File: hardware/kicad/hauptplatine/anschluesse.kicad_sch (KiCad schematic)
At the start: 9 parts, among them J701 DS18B20 Nr. 1, J702 DS18B20 Nr. 2, J703 BME280, J704 Erweiterung

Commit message: update
Footprints BQ25185, Ra-01SH, DEGSON 15EDGRC-3.5 (2-6P) in Bienen.pretty; HW-02 Akkuhalter Keystone 1042 SMD; SCH26-13 Klemmen einreihig mit LCSC-Nummern. Tests: ERC 0, Pin/Footprint 0 Abweichungen, Netzprüfung 178/178, alle_tests_linux.sh rc=0
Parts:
- J701, J702: footprint Connector_Phoenix_MC:PhoenixContact_MC_1,5_3-G-3.5_1x03_P3.50mm_Horizontal -> Bienen:DEGSON_15EDGRC-3.5-03P; LCSC (none) -> C5160226
- J703: footprint Connector_Phoenix_MC:PhoenixContact_MC_1,5_6-G-3.5_1x06_P3.50mm_Horizontal -> Bienen:DEGSON_15EDGRC-3.5-06P; LCSC (none) -> C49352918
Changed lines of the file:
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@@
 			)
 		)
-		(property "Footprint" "Connector_Phoenix_MC:PhoenixContact_MC_1,5_3-G-3.5_1x03_P3.50mm_Horizontal"
+		(property "Footprint" "Bienen:DEGSON_15EDGRC-3.5-03P"
 			(at 40.64 91.44 0)
 			(hide yes)
@@
 			)
 		)
-		(property "Description" "= J6 (TempIn): 1 GND, 2 DQ, 3 3V3_SW; DEGSON 15EDGRHC-3.5 3-polig (Platzhalter-Footprint Phoenix MC) [P]"
+		(property "Description" "= J6 (TempIn): 1 GND, 2 DQ, 3 3V3_SW; DEGSON 15EDGRC-3.5-03P"
+			(at 40.64 91.44 0)
+			(hide yes)
+			(show_name no)
+			(do_not_autoplace no)
+			(effects
+				(font
+					(size 1.27 1.27)
+				)
+			)
+		)
+		(property "LCSC" "C5160226"
 			(at 40.64 91.44 0)
 			(hide yes)
@@
 			)
 		)
-		(property "Footprint" "Connector_Phoenix_MC:PhoenixContact_MC_1,5_6-G-3.5_1x06_P3.50mm_Horizontal"
+		(property "Footprint" "Bienen:DEGSON_15EDGRC-3.5-06P"
 			(at 40.64 165.1 0)
 			(hide yes)
@@
 			)
 		)
-		(property "Description" "= J8: 1 Schirm, 2 GND, 3 SDA, 4 SCL, 5 3V3_SW, 6 frei (Verwechslungsschutz gegen J4, 6-polig); DEGSON 15EDGRHC-3.5 6-polig (Platzhalter-Footprint Phoenix MC) [P]"
+		(property "Description" "= J8: 1 Schirm, 2 GND, 3 SDA, 4 SCL, 5 3V3_SW, 6 frei (Verwechslungsschutz gegen J4, 6-polig); DEGSON 15EDGRC-3.5-06P"
+			(at 40.64 165.1 0)
+			(hide yes)
+			(show_name no)
+			(do_not_autoplace no)
+			(effects
+				(font
+					(size 1.27 1.27)
+				)
+			)
+		)
+		(property "LCSC" "C49352918"
 			(at 40.64 165.1 0)
 			(hide yes)
@@
 			)
 		)
-		(property "Footprint" "Connector_Phoenix_MC:PhoenixContact_MC_1,5_3-G-3.5_1x03_P3.50mm_Horizontal"
+		(property "Footprint" "Bienen:DEGSON_15EDGRC-3.5-03P"
 			(at 40.64 116.84 0)
 			(hide yes)
@@
 			)
 		)
-		(property "Description" "= J7 (TempIn2), selber Bus; DEGSON 15EDGRHC-3.5 3-polig (Platzhalter-Footprint Phoenix MC) [P]"
+		(property "Description" "= J7 (TempIn2), selber Bus; DEGSON 15EDGRC-3.5-03P"
 			(at 40.64 116.84 0)
 			(hide yes)
+			(show_name no)
+			(do_not_autoplace no)
+			(effects
+				(font
+					(size 1.27 1.27)
+				)
+			)
+		)
+		(property "LCSC" "C5160226"
+			(at 40.64 116.84 0)
+			(hide yes)

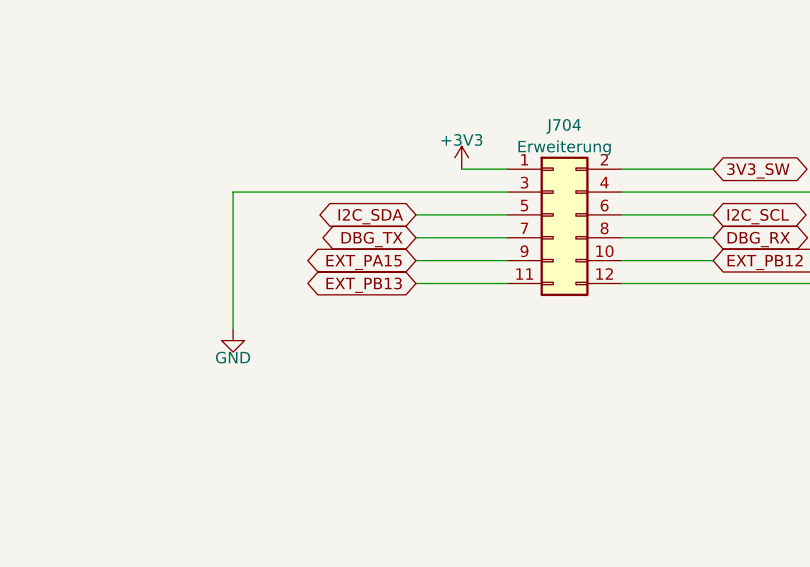
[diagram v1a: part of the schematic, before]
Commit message: HW-06: Akku auf der Hauptplatine (Blatt Akku, Akku-Platine entfällt); HW-05: USB mit VBUS-Erkennung an PB13; Routing-Werkzeuge; Aufräumen: Restbezüge Akku-Platine, README-Stand; ERC 0, Netzprüfung 168/168, Pin/Footprint 0; Platine platziert, nicht geroutet
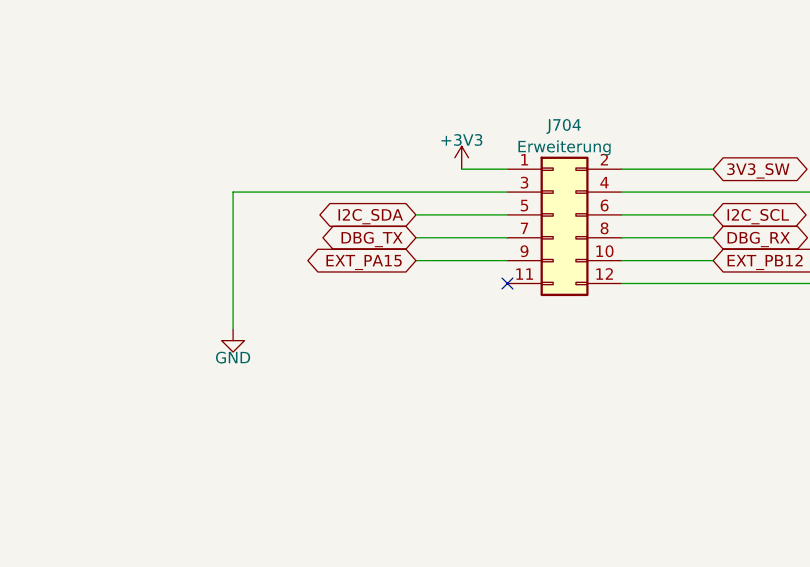
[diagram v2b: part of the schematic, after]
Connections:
- net EXT_PB13: no longer names the net of J704.11 (Pin_11)
- no-connect marks 4 -> 5

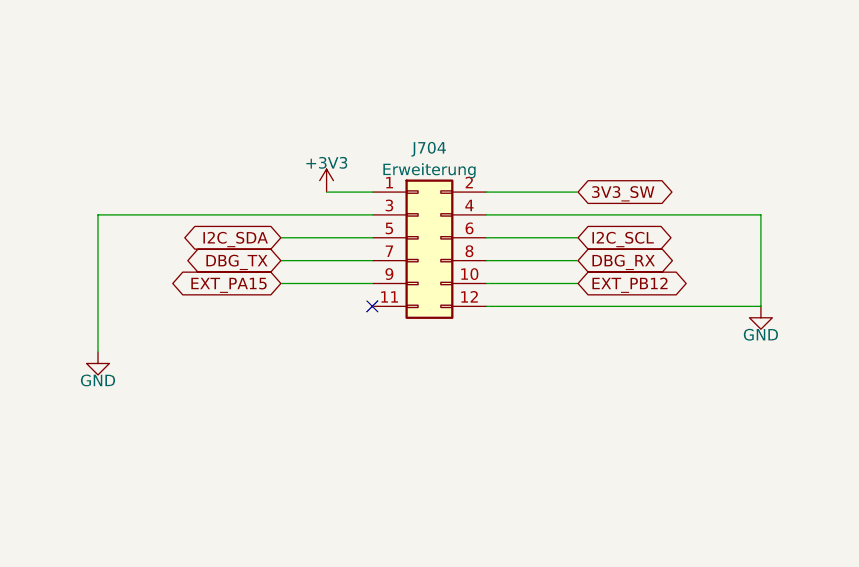
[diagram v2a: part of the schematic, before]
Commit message: HW-07: zwei Mikrofone am Audio-ADC TLV320ADC3101, I2S3, RJ45 J5; HW-08: Platine nur Rahmen, Layout extern; Pflichtenheft und Übergabepaket für den Layouter; ERC 0, Netzprüfung 187/187, Pin/Footprint 0
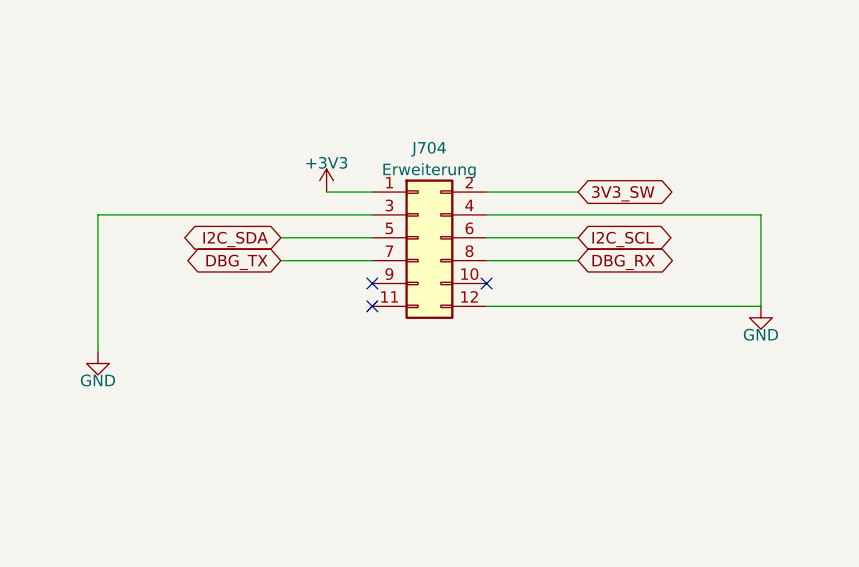
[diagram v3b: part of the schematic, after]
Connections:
- net EXT_PA15: no longer names the net of J704.9 (Pin_9)
- net EXT_PB12: no longer names the net of J704.10 (Pin_10)
- no-connect marks 5 -> 7
